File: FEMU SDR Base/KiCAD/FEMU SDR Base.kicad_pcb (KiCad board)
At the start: 4 copper layers, 164.8 x 164.8 mm, 31 parts, among them P2 SDR_Shield_1, P3 SDR_Shield_2, P8 Raspi_Power_Shield, U1 TPS562209, U2 SDR_1_LDO_1_2V, U3 SDR_2_LDO_1_2V, U4 SDR_1_LDO_3_3V, U5 SDR_2_LDO_3_3V

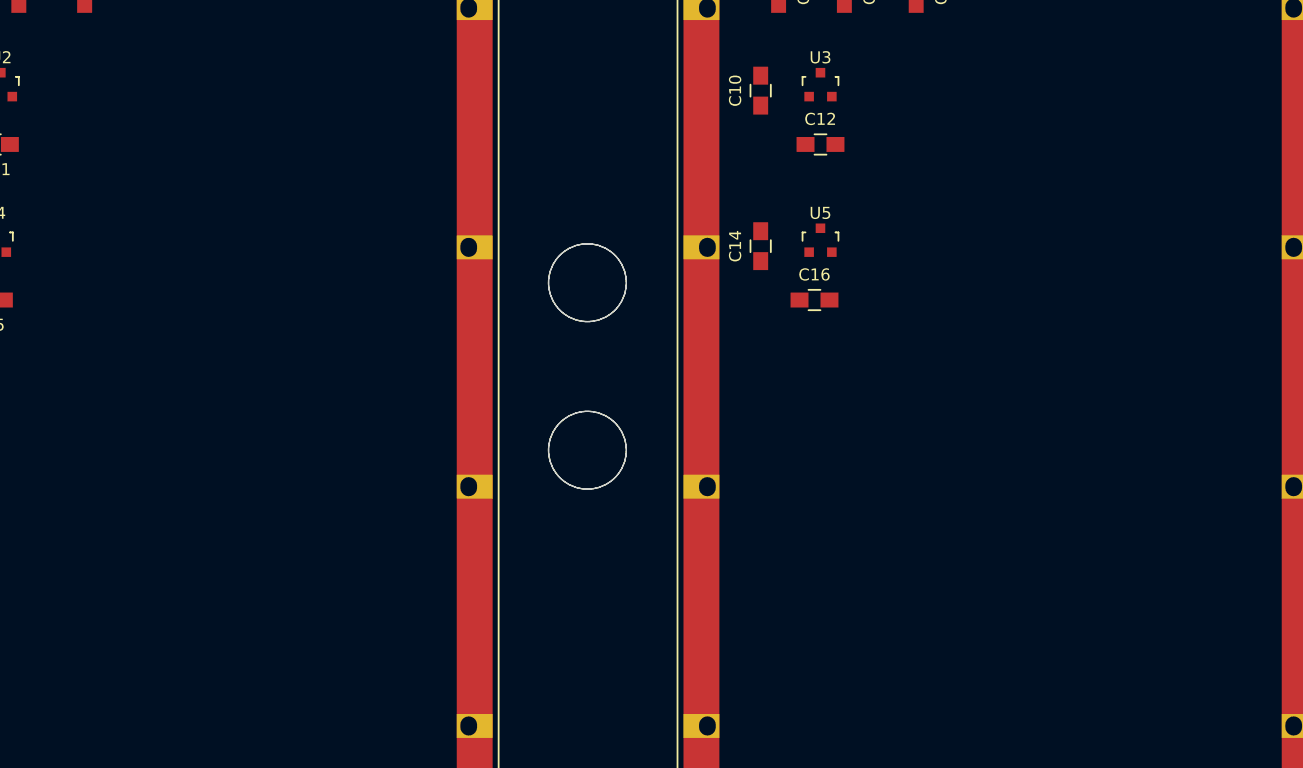
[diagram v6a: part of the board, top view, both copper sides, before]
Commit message: added hacked SDR outline
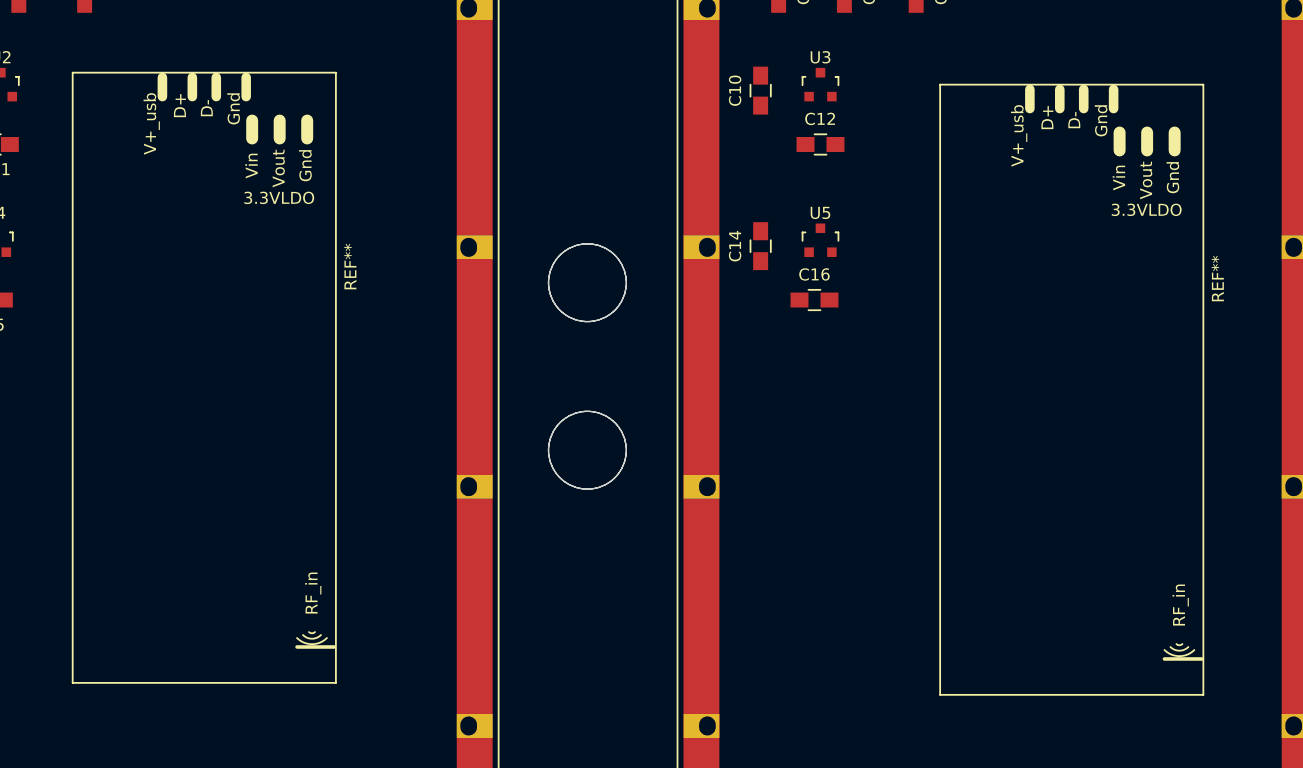
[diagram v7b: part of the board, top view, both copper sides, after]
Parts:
- added REF**: SDR_hack_outline, ARB_foots:SDR_hack_outline, F.Cu at (41.5, 111.0)
- added REF**: SDR_hack_outline, ARB_foots:SDR_hack_outline, F.Cu at (114.0, 112.0)
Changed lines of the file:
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@@
     (tracks 84)
     (zones 0)
-    (modules 31)
+    (modules 33)
     (nets 13)
   )
@@
       (net 8 GND))
   )
+  (module ARB_foots:SDR_hack_outline (layer F.Cu)
+    (at 41.5 111 90)
+    (fp_text reference REF** (at 34.75 23.25 90) (layer F.SilkS)
+      (effects (font (size 1 1) (thickness 0.15)))
+    )
+    (fp_text value SDR_hack_outline (at 31.25 -1.25 90) (layer F.Fab)
+      (effects (font (size 1 1) (thickness 0.15)))
+    )
+    (fp_text user 3.3VLDO (at 40.5 17.25 180) (layer F.SilkS)
+      (effects (font (size 1 1) (thickness 0.15)))
+    )
+    (fp_text user Gnd (at 43.25 19.5 90) (layer F.SilkS)
+      (effects (font (size 1 1) (thickness 0.15)))
+    )
+    (fp_text user Vout (at 43 17.25 90) (layer F.SilkS)
+      (effects (font (size 1 1) (thickness 0.15)))
+    )
+    (fp_text user Vin (at 43.25 15 90) (layer F.SilkS)
+      (effects (font (size 1 1) (thickness 0.15)))
+    )
+    (fp_line (start 47 19.6) (end 45.5 19.6) (layer F.SilkS) (width 1))
+    (fp_line (start 47 17.3) (end 45.5 17.3) (layer F.SilkS) (width 1))
+    (fp_line (start 47 15) (end 45.5 15) (layer F.SilkS) (width 1))
+    (fp_text user Gnd (at 48 13.5 90) (layer F.SilkS)
+      (effects (font (size 1 1) (thickness 0.15)))
+    )
+    (fp_text user D- (at 48 11.25 90) (layer F.SilkS)
+      (effects (font (size 1 1) (thickness 0.15)))
+    )
+    (fp_text user D+ (at 48.25 9 90) (layer F.SilkS)
+      (effects (font (size 1 1) (thickness 0.15)))
+    )
+    (fp_text user V+_usb (at 46.75 6.5 90) (layer F.SilkS)
+      (effects (font (size 1 1) (thickness 0.15)))
+    )
+    (fp_line (start 50.6 12) (end 49 12) (layer F.SilkS) (width 0.8))
+    (fp_line (start 50.6 14.5) (end 49 14.5) (layer F.SilkS) (width 0.8))
+    (fp_line (start 50.6 10) (end 49 10) (layer F.SilkS) (width 0.8))
+    (fp_line (start 50.6 7.5) (end 49 7.5) (layer F.SilkS) (width 0.8))
+    (fp_arc (start 4.5 20) (end 4.25 20.25) (angle 90) (layer F.SilkS) (width 0.15))
+    (fp_arc (start 4.75 20) (end 4 20.75) (angle 90) (layer F.SilkS) (width 0.15))
+    (fp_arc (start 5 20) (end 3.75 21.25) (angle 90) (layer F.SilkS) (width 0.15))
+    (fp_text user RF_in (at 7.5 20 90) (layer F.SilkS)
+      (effects (font (size 1 1) (thickness 0.15)))
+    )
+    (fp_line (start 3 21.85) (end 3 18.75) (layer F.SilkS) (width 0.3))
+    (fp_line (start 51 0) (end 51 22) (layer F.SilkS) (width 0.15))
+    (fp_line (start 51 22) (end 0 22) (layer F.SilkS) (width 0.15))
+    (fp_line (start 0 22) (end 0 0) (layer F.SilkS) (width 0.15))
+    (fp_line (start 0 0) (end 51 0) (layer F.SilkS) (width 0.15))
+  )
+  (module ARB_foots:SDR_hack_outline (layer F.Cu)
+    (at 114 112 90)
+    (fp_text reference REF** (at 34.75 23.25 90) (layer F.SilkS)
+      (effects (font (size 1 1) (thickness 0.15)))
+    )
+    (fp_text value SDR_hack_outline (at 31.25 -1.25 90) (layer F.Fab)
+      (effects (font (size 1 1) (thickness 0.15)))
+    )
+    (fp_text user 3.3VLDO (at 40.5 17.25 180) (layer F.SilkS)
+      (effects (font (size 1 1) (thickness 0.15)))
+    )
+    (fp_text user Gnd (at 43.25 19.5 90) (layer F.SilkS)
+      (effects (font (size 1 1) (thickness 0.15)))
+    )
+    (fp_text user Vout (at 43 17.25 90) (layer F.SilkS)
+      (effects (font (size 1 1) (thickness 0.15)))
+    )
+    (fp_text user Vin (at 43.25 15 90) (layer F.SilkS)
+      (effects (font (size 1 1) (thickness 0.15)))
+    )
+    (fp_line (start 47 19.6) (end 45.5 19.6) (layer F.SilkS) (width 1))
+    (fp_line (start 47 17.3) (end 45.5 17.3) (layer F.SilkS) (width 1))
+    (fp_line (start 47 15) (end 45.5 15) (layer F.SilkS) (width 1))
+    (fp_text user Gnd (at 48 13.5 90) (layer F.SilkS)
+      (effects (font (size 1 1) (thickness 0.15)))
+    )
+    (fp_text user D- (at 48 11.25 90) (layer F.SilkS)
+      (effects (font (size 1 1) (thickness 0.15)))
+    )
+    (fp_text user D+ (at 48.25 9 90) (layer F.SilkS)
+      (effects (font (size 1 1) (thickness 0.15)))
+    )
+    (fp_text user V+_usb (at 46.75 6.5 90) (layer F.SilkS)
+      (effects (font (size 1 1) (thickness 0.15)))
+    )
+    (fp_line (start 50.6 12) (end 49 12) (layer F.SilkS) (width 0.8))
+    (fp_line (start 50.6 14.5) (end 49 14.5) (layer F.SilkS) (width 0.8))
+    (fp_line (start 50.6 10) (end 49 10) (layer F.SilkS) (width 0.8))
+    (fp_line (start 50.6 7.5) (end 49 7.5) (layer F.SilkS) (width 0.8))
+    (fp_arc (start 4.5 20) (end 4.25 20.25) (angle 90) (layer F.SilkS) (width 0.15))
+    (fp_arc (start 4.75 20) (end 4 20.75) (angle 90) (layer F.SilkS) (width 0.15))
+    (fp_arc (start 5 20) (end 3.75 21.25) (angle 90) (layer F.SilkS) (width 0.15))
+    (fp_text user RF_in (at 7.5 20 90) (layer F.SilkS)
+      (effects (font (size 1 1) (thickness 0.15)))
+    )
+    (fp_line (start 3 21.85) (end 3 18.75) (layer F.SilkS) (width 0.3))
+    (fp_line (start 51 0) (end 51 22) (layer F.SilkS) (width 0.15))
+    (fp_line (start 51 22) (end 0 22) (layer F.SilkS) (width 0.15))
+    (fp_line (start 0 22) (end 0 0) (layer F.SilkS) (width 0.15))
+    (fp_line (start 0 0) (end 51 0) (layer F.SilkS) (width 0.15))
+  )
   (gr_line (start 25.9951 54.0536) (end 25.0811 54.0536) (layer Dwgs.User) (width 0.1))

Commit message: Planning and review
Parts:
- moved C1 4.30 mm to (84.3, 141.9)
- moved C2 4.30 mm to (81.6, 141.9)
- moved C3 4.30 mm to (92.6, 137.7)
- moved C4 4.30 mm to (80.6, 130.7)
- moved C5 4.30 mm to (80.6, 133.7)
- moved L1 4.30 mm to (76.3, 139.4)
- moved P8 4.30 mm to (84.8, 137.9)
- moved R1 4.30 mm to (89.1, 145.9)
- moved R2 4.30 mm to (90.1, 133.9)
- moved R3 4.30 mm to (95.3, 132.4)
- moved U1 4.30 mm to (89.3, 141.7)
